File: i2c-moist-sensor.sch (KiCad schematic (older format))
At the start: 21 parts, among them IC1 ATTINY441-SSU, P1 CONN_02X03, X1 16MHz

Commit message: New eeschema libs are new. Move TH1 and R4 OUT of the soil. Minimize stray capacitance where it matters
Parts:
- D3: symbol LED -> LED-RESCUE-i2c-moist-sensor
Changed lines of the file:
@@
 EESchema Schematic File Version 2
+LIBS:i2c-moist-sensor-rescue
 LIBS:power
 LIBS:device
@@
 Title "Digital soil moisture sensor"
 Date "Tue 17 Feb 2015"
-Rev ""
+Rev "2.7"
 Comp "Catnip electronics"
 Comment1 "by Albertas Mickėnas mic@wemakethings.net"
@@
 THERMISTOR
 $Comp
-L LED D3
+L LED-RESCUE-i2c-moist-sensor D3
 U 1 1 54E06E01
 P 5100 1550

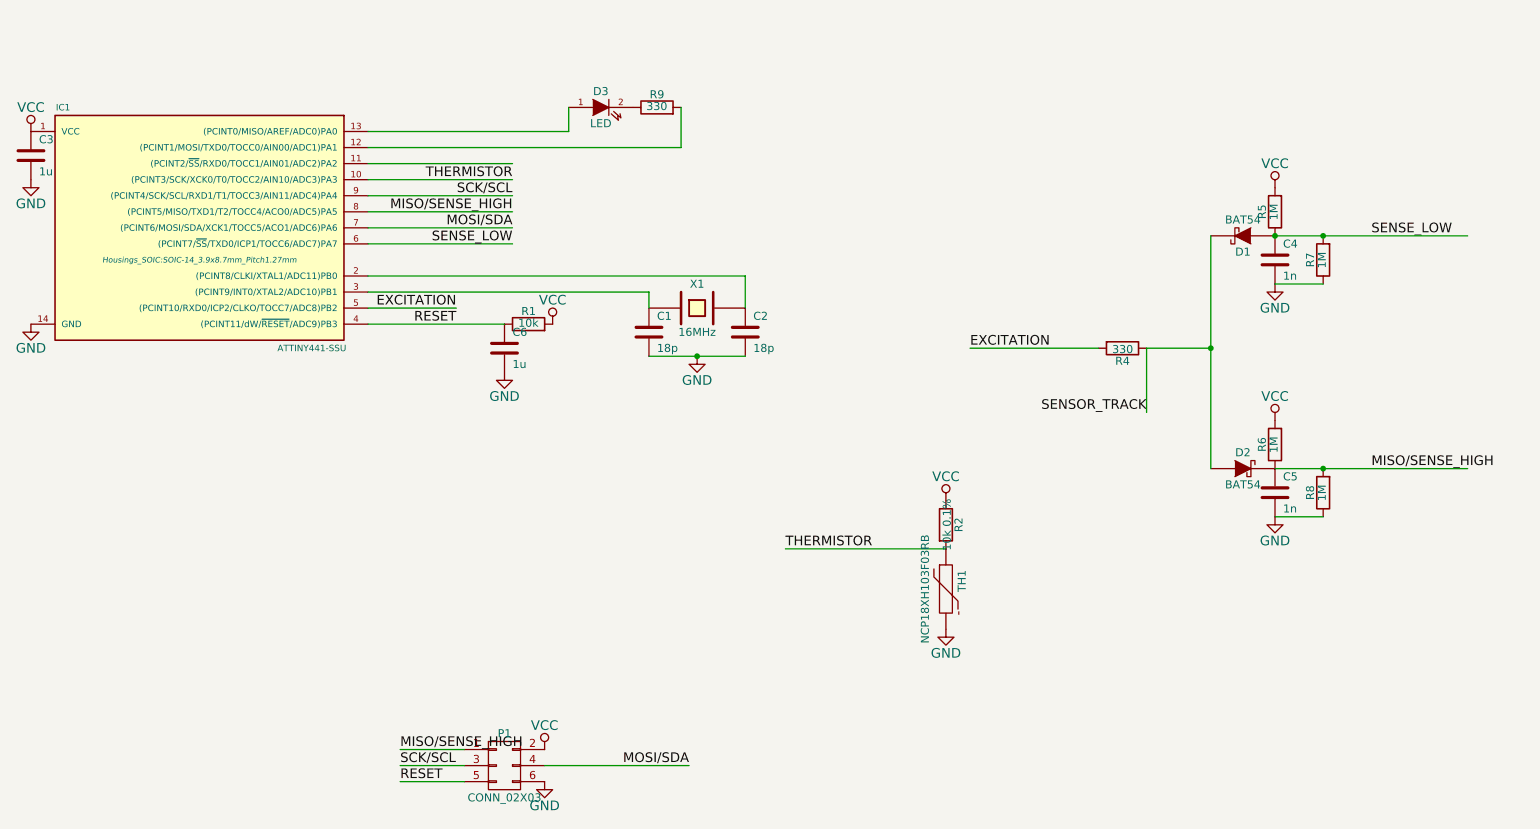
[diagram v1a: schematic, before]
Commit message: Fix LED footprint according to the datasheet, add data for the bom to schematics
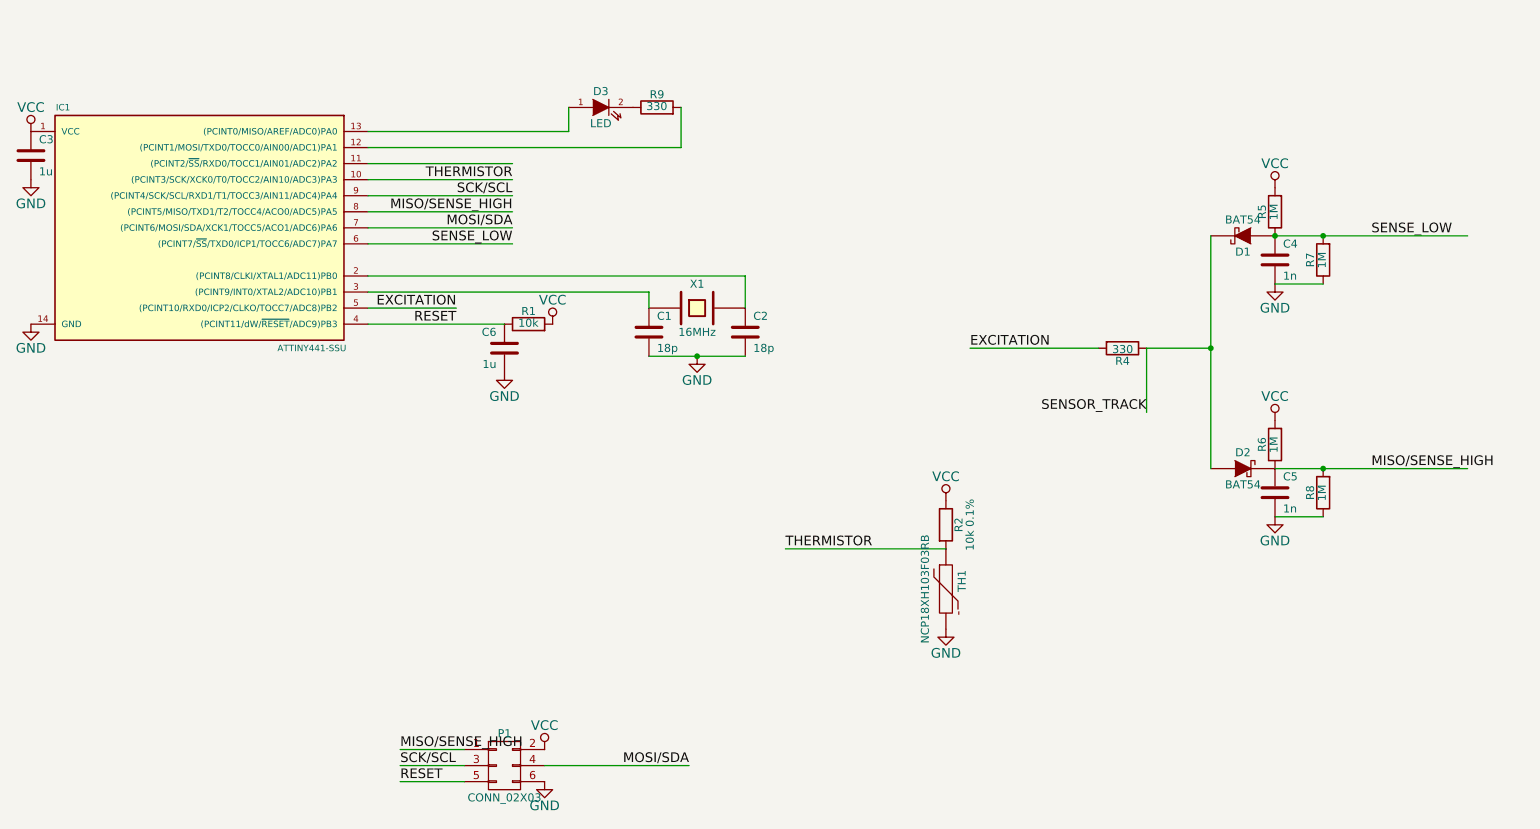
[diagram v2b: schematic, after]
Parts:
- C1, C2: Distributor (none) -> Farnell/2310585; Manufacturer (none) -> MULTICOMP; PartNo (none) -> MC0603N330J500CT
- C3, C6: Distributor (none) -> Farnell/2310637; Manufacturer (none) -> MULTICOMP; PartNo (none) -> MC0603X105K100CT
- C4, C5: Distributor (none) -> Farnell/2310598; Manufacturer (none) -> MULTICOMP; PartNo (none) -> MC0603B102K500CT
- D1, D2: Distributor (none) -> Farnell/2322476; Manufacturer (none) -> FAIRCHILD SEMICONDUCTOR; PartNo (none) -> BAT54XV2
- D3: Distributor (none) -> Farnell/2449786; Manufacturer (none) -> KINGBRIGHT; PartNo (none) -> KP-1608SURCK
- IC1: Distributor (none) -> Farnell/2396717; Manufacturer (none) -> ATMEL; PartNo (none) -> ATTINY441-SSU
- R1, R2: Distributor (none) -> Farnell/2379939; Manufacturer (none) -> PANASONIC ELECTRONIC COMPONENTS; PartNo (none) -> ERJ3RBD1002V
- R4, R9: Distributor (none) -> Farnell/2446656; Manufacturer (none) -> MULTICOMP; PartNo (none) -> MCWR06X3300FTL
- R5, R6, R7, R8: Distributor (none) -> Farnell/2446602; Manufacturer (none) -> MULTICOMP; PartNo (none) -> MCWR06X1004FTL
- TH1: Distributor (none) -> Farnell/2456122; Manufacturer (none) -> MURATA; PartNo (none) -> NCP18XH103F03RB
- X1: Distributor (none) -> Farnell/2395958; Manufacturer (none) -> MULTICOMP; PartNo (none) -> MCRSD16000F183000RR
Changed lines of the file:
@@
 F 2 "Crystals:Crystal_HC49-SD_SMD" H 5700 2800 60  0001 C CNN
 F 3 "" H 5700 2800 60  0000 C CNN
+F 4 "MULTICOMP" H 5700 2800 60  0001 C CNN "Manufacturer"
+F 5 " MCRSD16000F183000RR" H 5700 2800 60  0001 C CNN "PartNo"
+F 6 "Farnell/2395958" H 5700 2800 60  0001 C CNN "Distributor"
 	1    5700 2800
 	1    0    0    -1
@@
 F 2 "Capacitors_SMD:C_0603" H 5438 2800 30  0001 C CNN
 F 3 "" H 5400 2950 60  0000 C CNN
+F 4 "MULTICOMP" H 5400 2950 60  0001 C CNN "Manufacturer"
+F 5 " MC0603N330J500CT" H 5400 2950 60  0001 C CNN "PartNo"
+F 6 "Farnell/2310585" H 5400 2950 60  0001 C CNN "Distributor"
 	1    5400 2950
 	1    0    0    -1
@@
 F 2 "Capacitors_SMD:C_0603" H 6038 2800 30  0001 C CNN
 F 3 "" H 6000 2950 60  0000 C CNN
+F 4 "MULTICOMP" H 5400 2950 60  0001 C CNN "Manufacturer"
+F 5 " MC0603N330J500CT" H 5400 2950 60  0001 C CNN "PartNo"
+F 6 "Farnell/2310585" H 5400 2950 60  0001 C CNN "Distributor"
 	1    6000 2950
 	1    0    0    -1
@@
 F 2 "Capacitors_SMD:C_0603" H 1588 1700 30  0001 C CNN
 F 3 "" H 1550 1850 60  0000 C CNN
+F 4 " MC0603X105K100CT" H 1550 1850 60  0001 C CNN "PartNo"
+F 5 "MULTICOMP" H 1550 1850 60  0001 C CNN "Manufacturer"
+F 6 "Farnell/2310637" H 1550 1850 60  0001 C CNN "Distributor"
 	1    1550 1850
 	1    0    0    -1
@@
 F 2 "SMD_Packages:SOD-523" H 9100 2350 60  0001 C CNN
 F 3 "" H 9100 2350 60  0000 C CNN
+F 4 "BAT54XV2" H 9100 2350 60  0001 C CNN "PartNo"
+F 5 "FAIRCHILD SEMICONDUCTOR" H 9100 2350 60  0001 C CNN "Manufacturer"
+F 6 "Farnell/2322476" H 9100 2350 60  0001 C CNN "Distributor"
 	1    9100 2350
 	-1   0    0    1
@@
 F 2 "SMD_Packages:SOD-523" H 9100 3800 60  0001 C CNN
 F 3 "" H 9100 3800 60  0000 C CNN
+F 4 "BAT54XV2" H 9100 3800 60  0001 C CNN "PartNo"
+F 5 "FAIRCHILD SEMICONDUCTOR" H 9100 3800 60  0001 C CNN "Manufacturer"
+F 6 "Farnell/2322476" H 9100 3800 60  0001 C CNN "Distributor"
 	1    9100 3800
 	1    0    0    -1
@@
 F 2 "Resistors_SMD:R_0603" V 8280 3050 30  0001 C CNN
 F 3 "" H 8350 3050 30  0000 C CNN
+F 4 "MULTICOMP" V 8350 3050 60  0001 C CNN "Manufacturer"
+F 5 "MCWR06X3300FTL" V 8350 3050 60  0001 C CNN "PartNo"
+F 6 "Farnell/2446656" V 8350 3050 60  0001 C CNN "Distributor"
 	1    8350 3050
 	0    1    1    0
@@
 F 2 "Resistors_SMD:R_0603" V 9230 2200 30  0001 C CNN
 F 3 "" H 9300 2200 30  0000 C CNN
+F 4 "MCWR06X1004FTL" H 9300 2200 60  0001 C CNN "PartNo"
+F 5 "MULTICOMP" H 9300 2200 60  0001 C CNN "Manufacturer"
+F 6 "Farnell/2446602" H 9300 2200 60  0001 C CNN "Distributor"
 	1    9300 2200
 	-1   0    0    1
@@
 F 2 "Resistors_SMD:R_0603" V 9530 3950 30  0001 C CNN
 F 3 "" H 9600 3950 30  0000 C CNN
+F 4 "MCWR06X1004FTL" H 9600 3950 60  0001 C CNN "PartNo"
+F 5 "MULTICOMP" H 9600 3950 60  0001 C CNN "Manufacturer"
+F 6 "Farnell/2446602" H 9600 3950 60  0001 C CNN "Distributor"
 	1    9600 3950
 	-1   0    0    1
@@
 F 2 "Capacitors_SMD:C_0603" H 9338 2350 30  0001 C CNN
 F 3 "" H 9300 2500 60  0000 C CNN
+F 4 " MC0603B102K500CT" H 9300 2500 60  0001 C CNN "PartNo"
+F 5 "MULTICOMP" H 9300 2500 60  0001 C CNN "Manufacturer"
+F 6 "Farnell/2310598" H 9300 2500 60  0001 C CNN "Distributor"
 	1    9300 2500
 	1    0    0    -1
@@
 F 2 "Resistors_SMD:R_0603" V 9530 2500 30  0001 C CNN
 F 3 "" H 9600 2500 30  0000 C CNN
+F 4 "MCWR06X1004FTL" H 9600 2500 60  0001 C CNN "PartNo"
+F 5 "MULTICOMP" H 9600 2500 60  0001 C CNN "Manufacturer"
+F 6 "Farnell/2446602" H 9600 2500 60  0001 C CNN "Distributor"
 	1    9600 2500
 	-1   0    0    1
@@
 F 2 "Capacitors_SMD:C_0603" H 9338 3800 30  0001 C CNN
 F 3 "" H 9300 3950 60  0000 C CNN
+F 4 " MC0603B102K500CT" H 9300 3950 60  0001 C CNN "PartNo"
+F 5 "MULTICOMP" H 9300 3950 60  0001 C CNN "Manufacturer"
+F 6 "Farnell/2310598" H 9300 3950 60  0001 C CNN "Distributor"
 	1    9300 3950
 	1    0    0    -1
@@
 F 2 "Resistors_SMD:R_0603" V 9230 3650 30  0001 C CNN
 F 3 "" H 9300 3650 30  0000 C CNN
+F 4 "MCWR06X1004FTL" H 9300 3650 60  0001 C CNN "PartNo"
+F 5 "MULTICOMP" H 9300 3650 60  0001 C CNN "Manufacturer"
+F 6 "Farnell/2446602" H 9300 3650 60  0001 C CNN "Distributor"
 	1    9300 3650
 	-1   0    0    1
@@
 F 2 "Resistors_SMD:R_0603" V 4580 2900 30  0001 C CNN
 F 3 "" H 4650 2900 30  0000 C CNN
+F 4 "ERJ3RBD1002V" H 4650 2900 60  0001 C CNN "PartNo"
+F 5 "PANASONIC ELECTRONIC COMPONENTS" H 4650 2900 60  0001 C CNN "Manufacturer"
+F 6 "Farnell/2379939" H 4650 2900 60  0001 C CNN "Distributor"
 	1    4650 2900
 	0    -1   -1   0
@@
 F 2 "Capacitors_SMD:C_0603" H 4538 2900 30  0001 C CNN
 F 3 "" H 4500 3050 60  0000 C CNN
+F 4 " MC0603X105K100CT" H 4500 3050 60  0001 C CNN "PartNo"
+F 5 "MULTICOMP" H 4500 3050 60  0001 C CNN "Manufacturer"
+F 6 "Farnell/2310637" H 4500 3050 60  0001 C CNN "Distributor"
 	1    4500 3050
-	1    0    0    -1
+	-1   0    0    -1
 $EndComp
 $Comp
@@
 F 2 "Resistors_SMD:R_0603" H 7250 4550 60  0001 C CNN
 F 3 "" H 7250 4550 60  0000 C CNN
+F 4 "NCP18XH103F03RB" V 7250 4550 60  0001 C CNN "PartNo"
+F 5 "MURATA" V 7250 4550 60  0001 C CNN "Manufacturer"
+F 6 "Farnell/2456122" V 7250 4550 60  0001 C CNN "Distributor"
 	1    7250 4550
 	1    0    0    -1
@@
 P 7250 4150
 F 0 "R2" V 7330 4150 50  0000 C CNN
-F 1 "10k 0.1%" V 7257 4151 50  0000 C CNN
+F 1 "10k 0.1%" V 7400 4150 50  0000 C CNN
 F 2 "Resistors_SMD:R_0603" V 7180 4150 30  0001 C CNN
 F 3 "" H 7250 4150 30  0000 C CNN
+F 4 "PANASONIC ELECTRONIC COMPONENTS" V 7250 4150 60  0001 C CNN "Manufacturer"
+F 5 "ERJ3RBD1002V" V 7250 4150 60  0001 C CNN "PartNo"
+F 6 "Farnell/2379939" V 7250 4150 60  0001 C CNN "Distributor"
 	1    7250 4150
 	1    0    0    -1
@@
 F 2 "LEDs:LED-0603" H 5100 1550 60  0001 C CNN
 F 3 "" H 5100 1550 60  0000 C CNN
+F 4 "KINGBRIGHT" H 5100 1550 60  0001 C CNN "Manufacturer"
+F 5 "KP-1608SURCK" H 5100 1550 60  0001 C CNN "PartNo"
+F 6 "Farnell/2449786" H 5100 1550 60  0001 C CNN "Distributor"
 	1    5100 1550
 	1    0    0    -1
@@
 F 2 "Resistors_SMD:R_0603" V 5380 1550 30  0001 C CNN
 F 3 "" H 5450 1550 30  0000 C CNN
+F 4 " MCWR06X3300FTL" H 5450 1550 60  0001 C CNN "PartNo"
+F 5 "MULTICOMP" H 5450 1550 60  0001 C CNN "Manufacturer"
+F 6 "Farnell/2446656" H 5450 1550 60  0001 C CNN "Distributor"
 	1    5450 1550
 	0    -1   -1   0
@@
 F 0 "IC1" H 1750 3050 40  0000 C CNN
 F 1 "ATTINY441-SSU" H 3300 1550 40  0000 C CNN
-F 2 "Housings_SOIC:SOIC-14_3.9x8.7mm_Pitch1.27mm" H 2600 2100 35  0000 C CIN
+F 2 "Housings_SOIC:SOIC-14_3.9x8.7mm_Pitch1.27mm" H 2600 2100 35  0001 C CIN
 F 3 "" H 2600 2300 60  0000 C CNN
+F 4 "ATTINY441-SSU" H 2600 2300 60  0001 C CNN "PartNo"
+F 5 "ATMEL" H 2600 2300 60  0001 C CNN "Manufacturer"
+F 6 "Farnell/2396717" H 2600 2300 60  0001 C CNN "Distributor"
 	1    2600 2300
 	1    0    0    -1

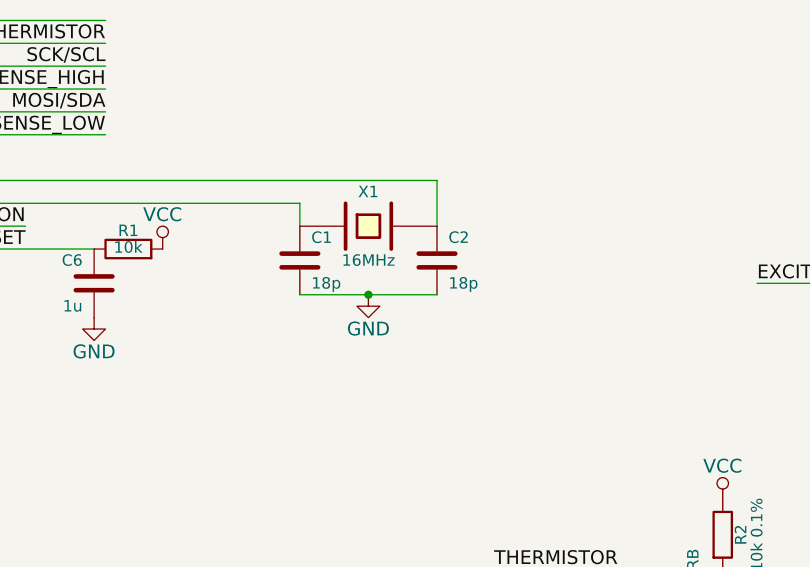
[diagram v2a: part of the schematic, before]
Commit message: Change xtal load cap value
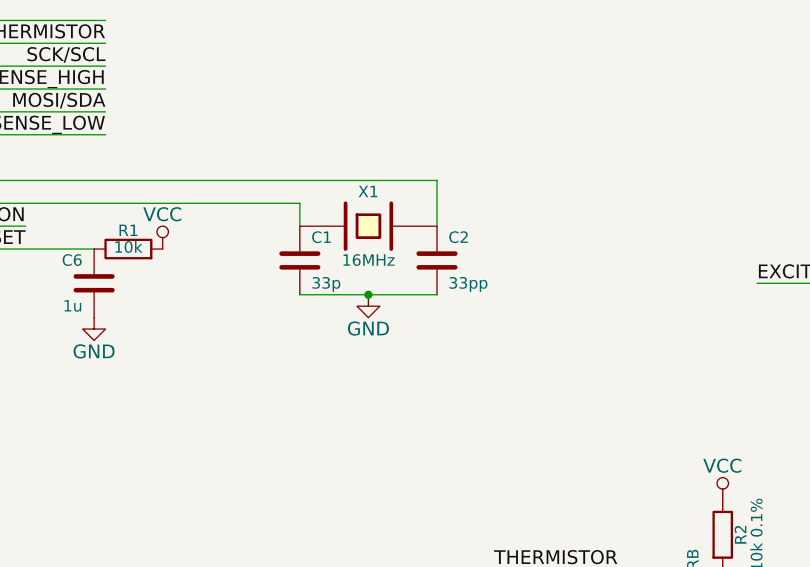
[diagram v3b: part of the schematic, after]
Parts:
- C1: value 18p -> 33p
- C2: value 18p -> 33pp
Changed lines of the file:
@@
 Sheet 1 1
 Title "Digital soil moisture sensor"
-Date "Tue 17 Feb 2015"
-Rev "2.7"
+Date "2015-10-26"
+Rev "2.7.3"
 Comp "Catnip electronics"
 Comment1 "by Albertas Mickėnas mic@wemakethings.net"
@@
 P 5400 2950
 F 0 "C1" H 5450 3050 50  0000 L CNN
-F 1 "18p" H 5450 2850 50  0000 L CNN
+F 1 "33p" H 5450 2850 50  0000 L CNN
 F 2 "Capacitors_SMD:C_0603" H 5438 2800 30  0001 C CNN
 F 3 "" H 5400 2950 60  0000 C CNN
@@
 P 6000 2950
 F 0 "C2" H 6050 3050 50  0000 L CNN
-F 1 "18p" H 6050 2850 50  0000 L CNN
+F 1 "33pp" H 6050 2850 50  0000 L CNN
 F 2 "Capacitors_SMD:C_0603" H 6038 2800 30  0001 C CNN
 F 3 "" H 6000 2950 60  0000 C CNN
